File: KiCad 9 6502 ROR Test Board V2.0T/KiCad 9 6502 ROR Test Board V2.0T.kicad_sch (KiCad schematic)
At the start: 29 parts, among them P1 CONN-TH_2P-P5.00, Q1 2N7000, Q2 2N7000, U1 6502, U2 AT28C256, U3 SN74HCT14N, U4 SN74LS74AN, U5 Plated Through Hole M3, U6 Plated Through Hole M3, U7 Plated Through Hole M3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

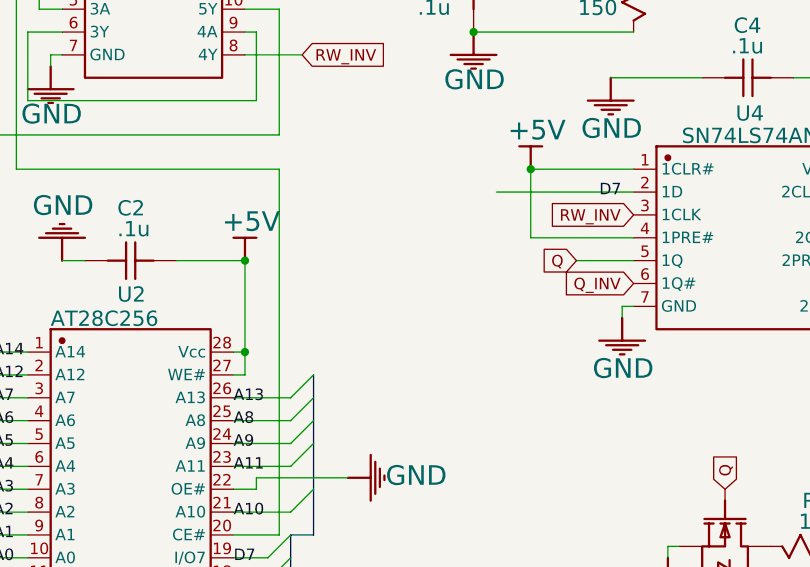
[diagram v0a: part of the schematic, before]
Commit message: added 3D models to KiCad
Added 3D Models of components to both KiCad Boards

Fixed footprint of screw terminal to match with 30.702 on both easyeda and kicad files

re-rendered 2D view from EasyEDA and  added 3D view rendering from KiCad

Renders in separate folder

Exported new gerbers from both EasyEDA and KiCad with updated footprint

Exported 3D model of both boards from KiCad and added to folder.

Updated link to smd LED to active part.
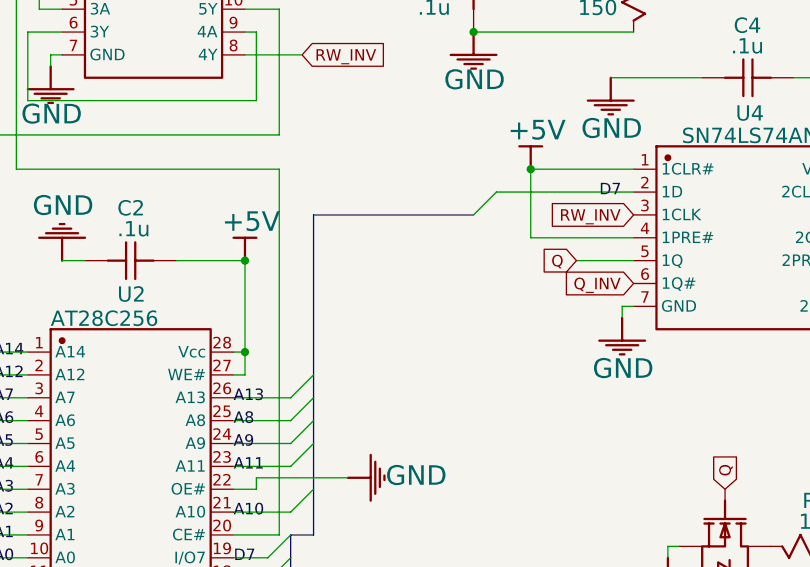
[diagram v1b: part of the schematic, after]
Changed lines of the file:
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@@
+	)
+	(bus_entry
+		(at 214.63 87.63)
+		(size -2.54 2.54)
+		(stroke
+			(width 0)
+			(type default)
+		)
 	)
 	(bus_entry
@@
 	(bus
 		(pts
+			(xy 194.31 90.17) (xy 212.09 90.17)
+		)
+		(stroke
+			(width 0)
+			(type default)
+		)
+	)
+	(bus
+		(pts
 			(xy 191.77 125.73) (xy 191.77 128.27)
 		)
@@
 		)
 		(stroke
+			(width 0)
+			(type default)
+		)
+	)
+	(bus
+		(pts
+			(xy 194.31 107.95) (xy 194.31 90.17)
+		)
+		(stroke
